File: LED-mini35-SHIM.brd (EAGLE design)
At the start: 50.8 x 12.7 mm, 19 parts, among them IC1 TXB0101DCKR

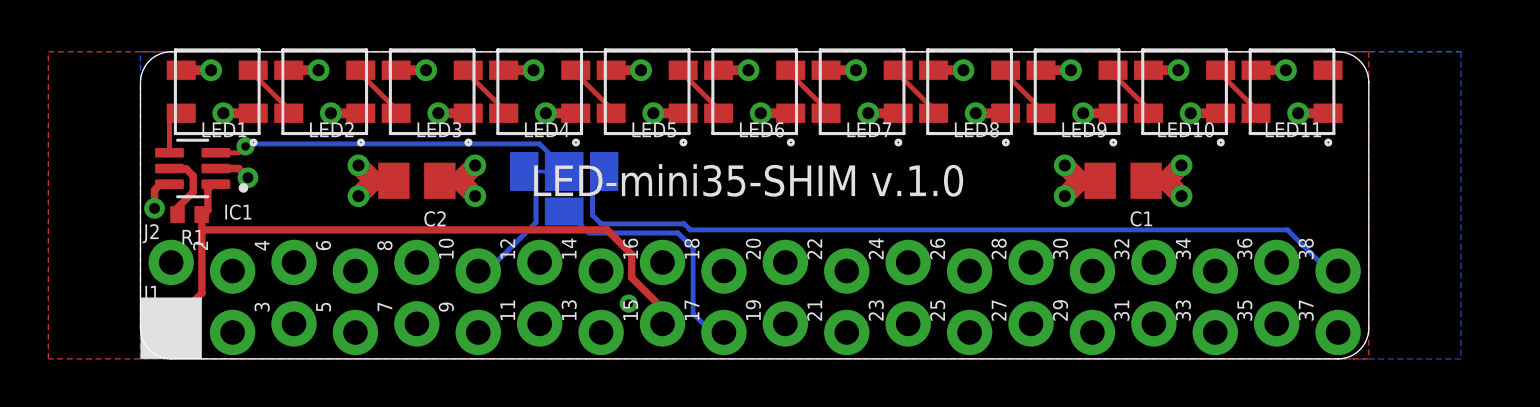
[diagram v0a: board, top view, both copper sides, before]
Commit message: Added one more 35mm LED to the mini-board. Generated CAM files. Generated PDF schematics. Generated PNG preview.
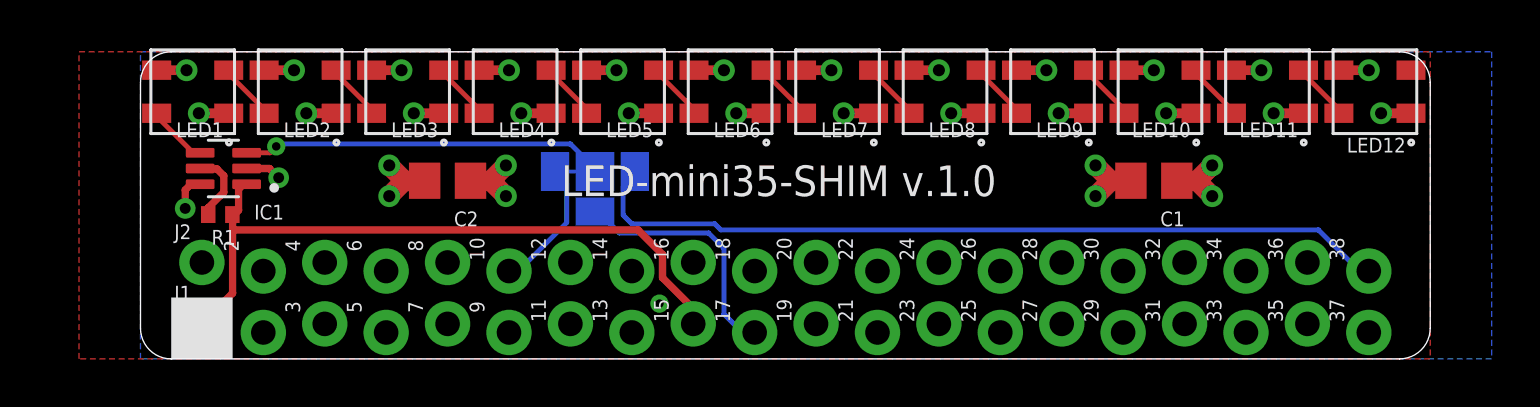
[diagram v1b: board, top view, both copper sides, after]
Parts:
- added LED12: WS2812B-MINI, WS281X:WS2812X-MINI
- moved IC1 1.27 mm to (3.43, 7.87)
- moved J1 1.27 mm to (2.54, 1.27)
- moved J2 1.27 mm to (2.54, 3.81)
- moved R1 1.27 mm to (3.30, 5.97)
- moved C2 1.27 mm to (12.7, 7.37)
- moved SJ1 1.27 mm to (18.8, 7.75)
- moved C1 1.27 mm to (41.9, 7.37)
- moved LOGO1 1.27 mm to (54.5, 0.51)
- moved LED4 1.02 mm to (15.5, 11.0)
- moved LED1 1.02 mm to (2.16, 11.0)
- moved LED2 1.02 mm to (6.60, 11.0)
- moved LED3 1.02 mm to (11.0, 11.0)
- moved LED10 1.02 mm to (42.2, 11.0)
- moved LED11 1.02 mm to (46.6, 11.0)
- moved LED5 1.02 mm to (19.9, 11.0)
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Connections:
- new net N$11: LED11.DO, LED12.DI
- net 5V: now also LED12.VDD
- net DO_LAST: now also LED12.DO; no longer LED11.DO
- net GND: now also LED12.GND
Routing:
- net N$11: track 0.00 -> 2.39 mm
- net 5V: track 20.3 -> 21.6 mm, vias 17 -> 18
- net GND: track 20.3 -> 21.6 mm, vias 16 -> 17
- net DI_FIRST: track 1.91 -> 2.73 mm
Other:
- board size 50.8 x 12.7 mm -> 53.3 x 12.7 mm

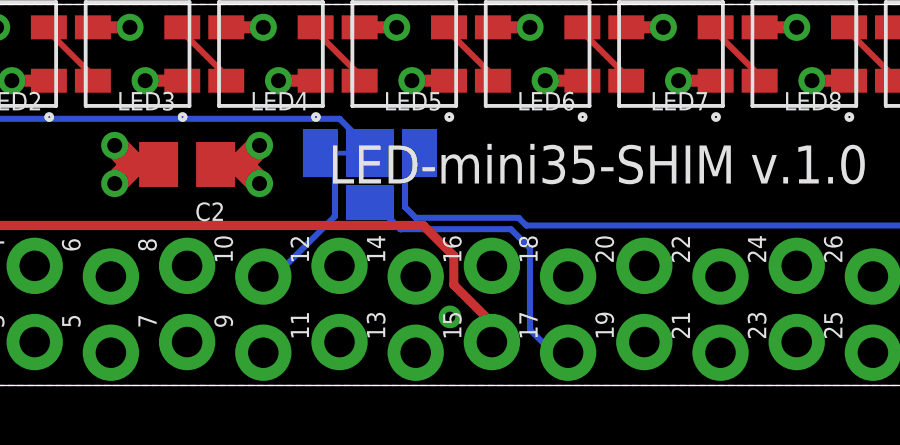
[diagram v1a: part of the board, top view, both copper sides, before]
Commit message: Fixed VIA. Generated CAM files. Generated PNG preview. Renamed BoM and PnP files.
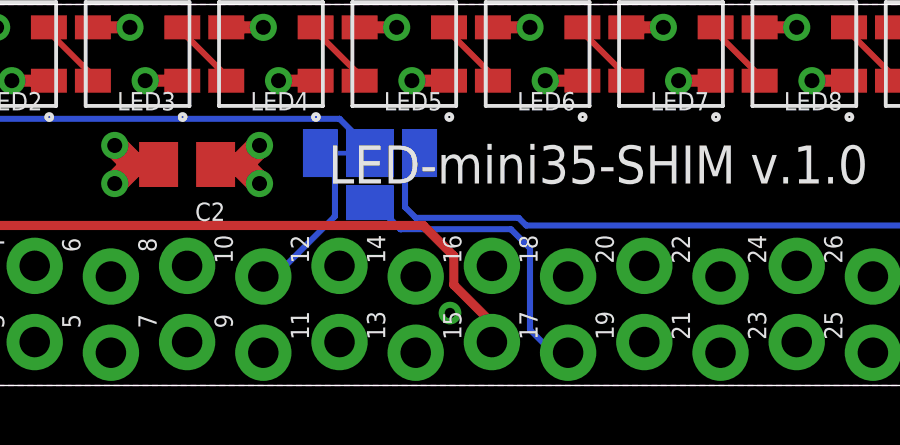
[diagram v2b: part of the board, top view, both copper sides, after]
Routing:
- net GND: vias 17 -> 18
- net 5V: vias 18 -> 17
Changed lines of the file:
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@@
 <drawing>
 <settings>
-<setting alwaysvectorfont="yes"/>
+<setting alwaysvectorfont="no"/>
 <setting verticaltext="up"/>
 </settings>
@@
 <wire x1="50.799" y1="11.939" x2="50.8" y2="11.938" width="0.4064" layer="1"/>
 <via x="50.8" y="11.938" extent="1-16" drill="0.5"/>
+<via x="21.463" y="2.413" extent="1-16" drill="0.35"/>
 </signal>
 <signal name="GPIO2">
@@
 <wire x1="43.688" y1="7.366" x2="44.323" y2="8.001" width="0.8128" layer="1"/>
 <via x="44.323" y="8.001" extent="1-16" drill="0.5"/>
-<via x="21.463" y="2.286" extent="1-16" drill="0.35"/>
 <wire x1="3.649" y1="10.159" x2="2.414" y2="10.159" width="0.4064" layer="1"/>
 <wire x1="2.414" y1="10.159" x2="2.413" y2="10.16" width="0.4064" layer="1"/>
